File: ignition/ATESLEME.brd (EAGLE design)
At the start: 30.3 x 53.7 mm, 54 parts, among them U1 ADXL345PATRICK, U7 AMS1117-3.3

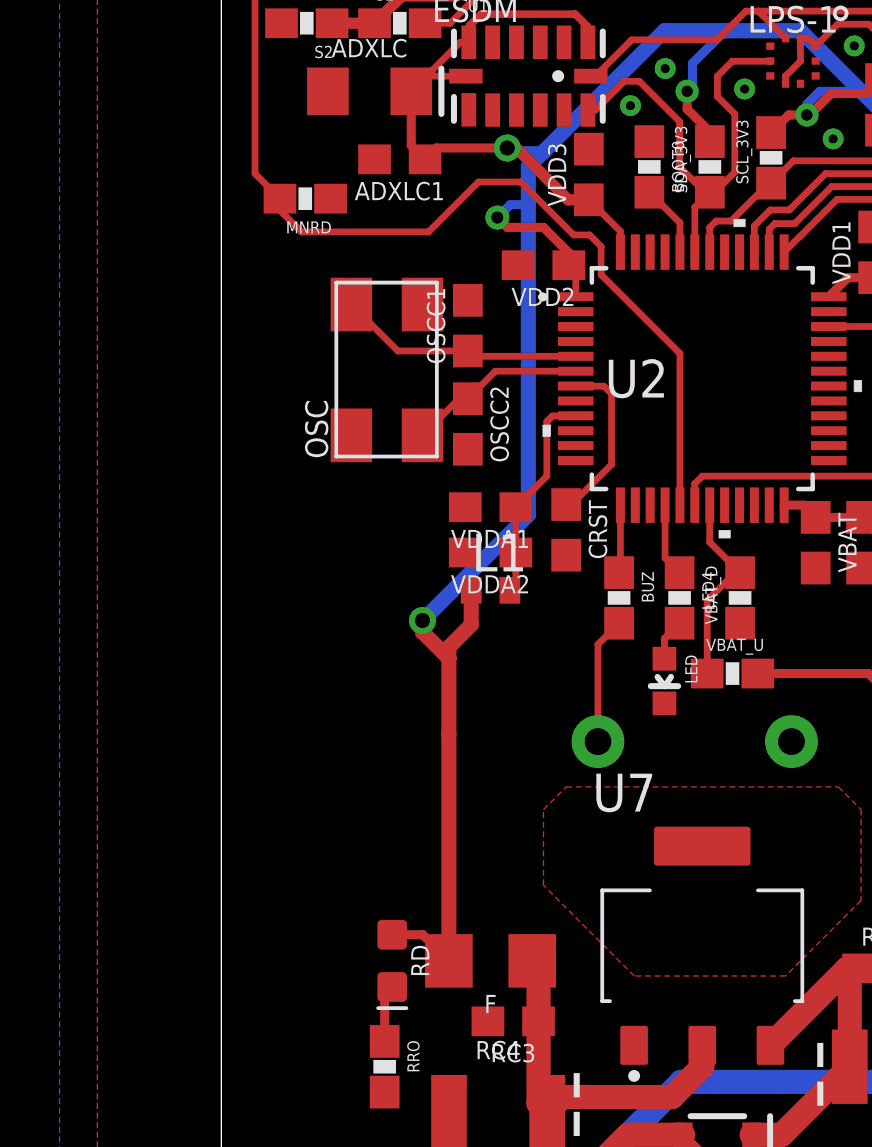
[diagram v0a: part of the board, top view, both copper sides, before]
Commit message: Guard ring was located around of HSE crystal
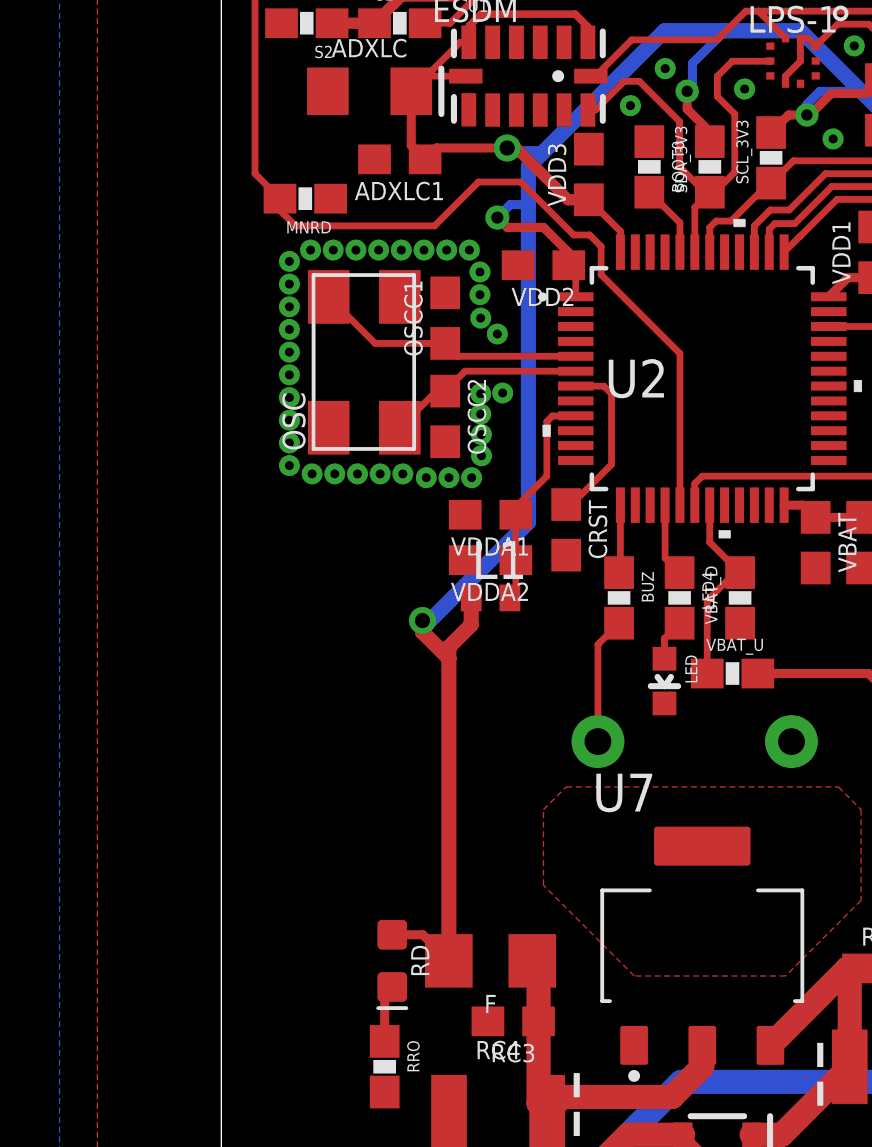
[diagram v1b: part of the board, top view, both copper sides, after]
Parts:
- moved OSCC1 0.80 mm to (11.7, 34.3)
- moved OSCC2 0.80 mm to (11.7, 31.0)
- moved OSC 0.80 mm to (8.89, 32.8)
- moved L1 0.25 mm to (13.2, 24.9)
- moved VDDA1 0.25 mm to (13.2, 27.7)
- moved VDDA2 0.25 mm to (13.2, 26.2)
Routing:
- net OSC_ıN: track 8.26 -> 9.12 mm
- net OSC_OUT: track 6.04 -> 6.70 mm

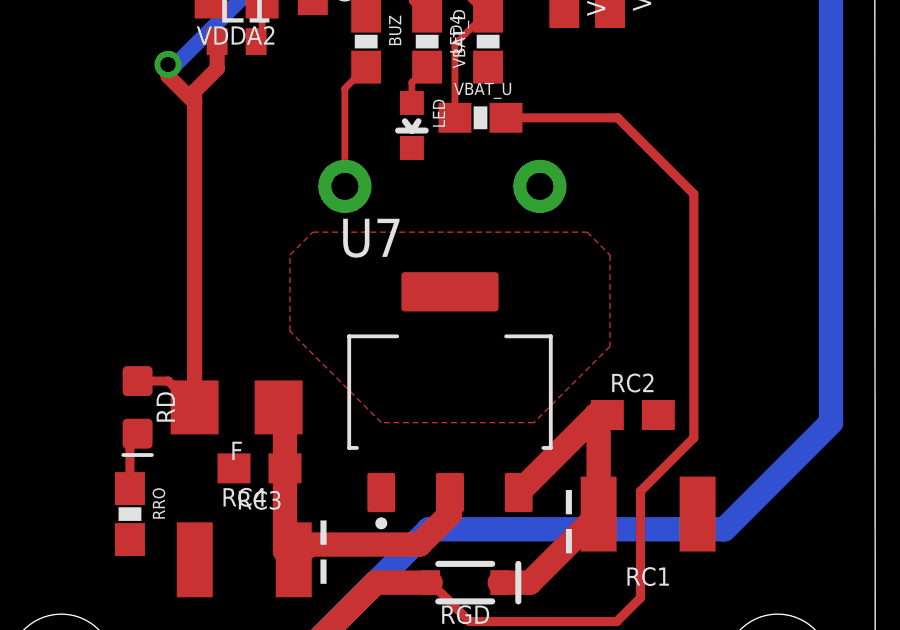
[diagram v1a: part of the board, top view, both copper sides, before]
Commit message: Discrite polygon was applied to heat pad of AMS1117-3.3
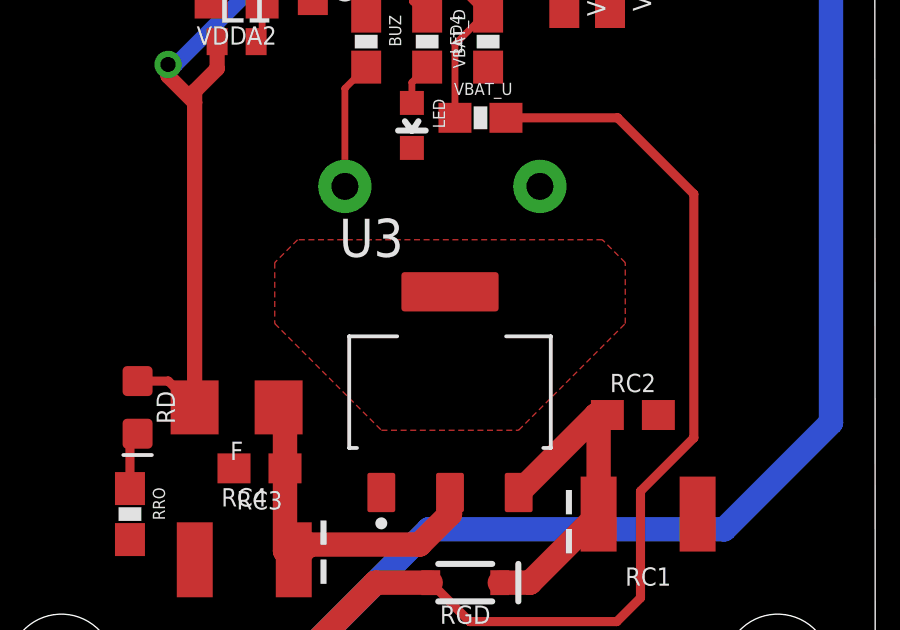
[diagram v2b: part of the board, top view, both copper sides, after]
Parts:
- renumbered U7 to U3
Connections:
- new net HT: U3.4
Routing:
- added copper zone on layer 1, net HT
- removed copper zone on layer 1, net HEAT
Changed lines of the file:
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@@
 <drawing>
 <settings>
-<setting alwaysvectorfont="yes"/>
+<setting alwaysvectorfont="no"/>
 <setting verticaltext="up"/>
 </settings>
-<grid distance="10" unitdist="mil" unit="mm" style="lines" multiple="1" display="yes" altdistance="1" altunitdist="mil" altunit="mm"/>
+<grid distance="10" unitdist="mil" unit="mil" style="lines" multiple="1" display="yes" altdistance="1" altunitdist="mil" altunit="mil"/>
 <layers>
 <layer number="1" name="Top" color="4" fill="1" visible="yes" active="yes"/>
@@
 <attribute name="VENDOR" value="STMicroelectronics" x="39.37" y="11.938" size="1.778" layer="27" display="off"/>
 </element>
-<element name="U7" library="AMS1117-3.3" package="SOT229P700X180-4N" value="AMS1117-3.3" x="20.32" y="13.208" smashed="yes">
-<attribute name="AVAILABILITY" value="Unavailable" x="40.64" y="5.588" size="1.778" layer="27" display="off"/>
-<attribute name="DESCRIPTION" value=" Sot223/Pkg 1-Amp 3.3-Volt Low Drop Out Voltage Regulatator " x="40.64" y="5.588" size="1.778" layer="27" display="off"/>
-<attribute name="MF" value="Advanced Monolithic Systems" x="40.64" y="5.588" size="1.778" layer="27" display="off"/>
-<attribute name="MP" value="AMS1117-3.3" x="40.64" y="5.588" size="1.778" layer="27" display="off"/>
-<attribute name="NAME" x="16.62345" y="17.715990625" size="1.27225" layer="25"/>
-<attribute name="PACKAGE" value="SOT-89 ams" x="40.64" y="5.588" size="1.778" layer="27" display="off"/>
-<attribute name="PRICE" value="None" x="40.64" y="5.588" size="1.778" layer="27" display="off"/>
-<attribute name="VALUE" x="16.623440625" y="7.03705" size="1.272259375" layer="27"/>
-</element>
 <element name="U8" library="IRLML6344TRPBF" package="SOT95P240X112-3N" value="" x="25.908" y="48.26" smashed="yes" rot="R90">
 <attribute name="AVAILABILITY" value="Good" x="62.738" y="71.12" size="1.778" layer="27" rot="R90" display="off"/>
@@
 <attribute name="VALUE" x="13.208" y="26.924" size="0.6096" layer="27" font="vector" ratio="20" rot="R180" align="top-center"/>
 </element>
+<element name="U3" library="AMS1117-3.3" library_urn="urn:adsk.eagle:library:27162810" package="SOT229P700X180-4N" package3d_urn="urn:adsk.eagle:package:27162813/2" value="AMS1117-3.3" x="20.32" y="13.208" smashed="yes">
+<attribute name="AVAILABILITY" value="Unavailable" x="20.32" y="13.208" size="1.778" layer="27" display="off"/>
+<attribute name="DESCRIPTION" value=" Sot223/Pkg 1-Amp 3.3-Volt Low Drop Out Voltage Regulatator " x="20.32" y="13.208" size="1.778" layer="27" display="off"/>
+<attribute name="MF" value="Advanced Monolithic Systems" x="20.32" y="13.208" size="1.778" layer="27" display="off"/>
+<attribute name="MP" value="AMS1117-3.3" x="20.32" y="13.208" size="1.778" layer="27" display="off"/>
+<attribute name="NAME" x="16.62345" y="17.715990625" size="1.27225" layer="25"/>
+<attribute name="PACKAGE" value="SOT-89 ams" x="20.32" y="13.208" size="1.778" layer="27" display="off"/>
+<attribute name="PRICE" value="None" x="20.32" y="13.208" size="1.778" layer="27" display="off"/>
+<attribute name="VALUE" x="16.623440625" y="7.03705" size="1.272259375" layer="27"/>
+</element>
 </elements>
 <signals>
@@
 <contactref element="RC1" pad="C"/>
 <contactref element="RC2" pad="2"/>
-<contactref element="U7" pad="1"/>
 <contactref element="RC3" pad="2"/>
 <contactref element="RC4" pad="C"/>
@@
 <via x="13.6144" y="31.7754" extent="1-16" drill="0.3"/>
 <via x="13.4366" y="33.7566" extent="1-16" drill="0.3"/>
+<contactref element="U3" pad="1"/>
 </signal>
 <signal name="VCC">
@@
 </signal>
 <signal name="VNR">
-<contactref element="U7" pad="3"/>
 <contactref element="RC1" pad="A"/>
 <contactref element="RC2" pad="1"/>
 <contactref element="RGD" pad="C"/>
-<wire x1="22.61" y1="9.863" x2="25.193" y2="12.446" width="0.8128" layer="1"/>
 <wire x1="25.193" y1="12.446" x2="25.566" y2="12.446" width="0.8128" layer="1"/>
 <wire x1="21.978" y1="6.858" x2="22.988" y2="6.858" width="0.8128" layer="1"/>
@@
 <wire x1="25.274" y1="9.144" x2="25.274" y2="12.154" width="0.8128" layer="1"/>
 <wire x1="25.274" y1="12.154" x2="25.566" y2="12.446" width="0.8128" layer="1"/>
+<contactref element="U3" pad="3"/>
+<wire x1="22.61" y1="9.863" x2="25.193" y2="12.446" width="0.8128" layer="1"/>
 </signal>
 <signal name="N$1">
-<contactref element="U7" pad="2"/>
 <contactref element="RC4" pad="A"/>
 <contactref element="RC3" pad="1"/>
@@
 <wire x1="15.112" y1="7.62" x2="15.62" y2="8.128" width="0.8128" layer="1"/>
 <wire x1="15.62" y1="8.128" x2="19.304" y2="8.128" width="0.8128" layer="1"/>
-<wire x1="19.304" y1="8.128" x2="20.32" y2="9.144" width="0.8128" layer="1"/>
-<wire x1="20.32" y1="9.144" x2="20.32" y2="9.863" width="0.8128" layer="1"/>
 <wire x1="14.82" y1="10.668" x2="14.82" y2="7.912" width="0.8128" layer="1"/>
 <wire x1="14.82" y1="7.912" x2="15.112" y2="7.62" width="0.8128" layer="1"/>
 <wire x1="14.82" y1="10.668" x2="14.82" y2="12.488" width="0.8128" layer="1"/>
 <wire x1="14.82" y1="12.488" x2="14.608" y2="12.7" width="0.8128" layer="1"/>
+<contactref element="U3" pad="2" route="any" routetag="G$1.VOUT"/>
+<wire x1="19.304" y1="8.128" x2="20.32" y2="9.144" width="0.8128" layer="1"/>
+<wire x1="20.32" y1="9.144" x2="20.32" y2="9.863" width="0.8128" layer="1"/>
 </signal>
 <signal name="3.3V">
@@
 <wire x1="19.07" y1="26.23" x2="19.558" y2="25.742" width="0.2286" layer="1"/>
 </signal>
-<signal name="HEAT">
+<signal name="HT">
+<contactref element="U3" pad="4"/>
 <polygon width="0.1524" layer="1">
-<vertex x="18.034" y="12.192"/>
-<vertex x="14.986" y="15.24"/>
-<vertex x="14.986" y="17.78"/>
-<vertex x="15.748" y="18.542"/>
-<vertex x="24.892" y="18.542"/>
-<vertex x="25.654" y="17.78"/>
-<vertex x="25.654" y="14.732"/>
-<vertex x="23.114" y="12.192"/>
+<vertex x="18.034" y="11.938"/>
+<vertex x="22.606" y="11.938"/>
+<vertex x="26.162" y="15.494"/>
+<vertex x="26.162" y="17.526"/>
+<vertex x="25.4" y="18.288"/>
+<vertex x="15.24" y="18.288"/>
+<vertex x="14.478" y="17.526"/>
+<vertex x="14.478" y="15.494"/>
 </polygon>
 </signal>
